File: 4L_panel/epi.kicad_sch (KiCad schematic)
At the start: 31 parts, among them J1 Connector 1x12, J2 Connector 1x12, J3 Conn_01x05, J4 USB-C 2.0 mid-mount female co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, U1 ATmega32U4-M, Y1 Crystal_GND24

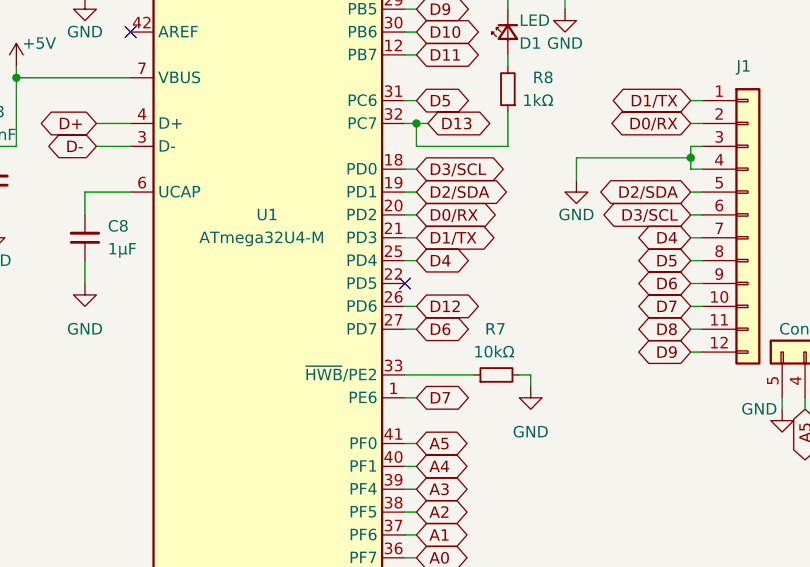
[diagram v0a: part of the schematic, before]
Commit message: minor design changes and pinout diagram added
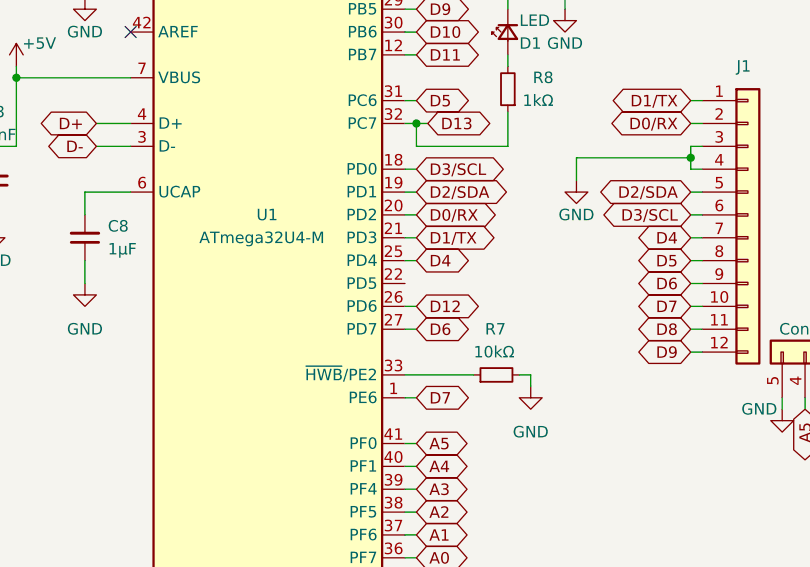
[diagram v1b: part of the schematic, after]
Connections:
- no-connect marks 6 -> 5
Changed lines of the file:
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@@
   )
   (no_connect (at 168.91 22.86))
-  (no_connect (at 73.66 81.28))
   (no_connect (at 191.77 15.24))
   (no_connect (at 43.18 53.34))
